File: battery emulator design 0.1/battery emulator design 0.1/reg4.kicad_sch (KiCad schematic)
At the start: 12 parts, among them U7 LM741, U8 LM317_TO-220

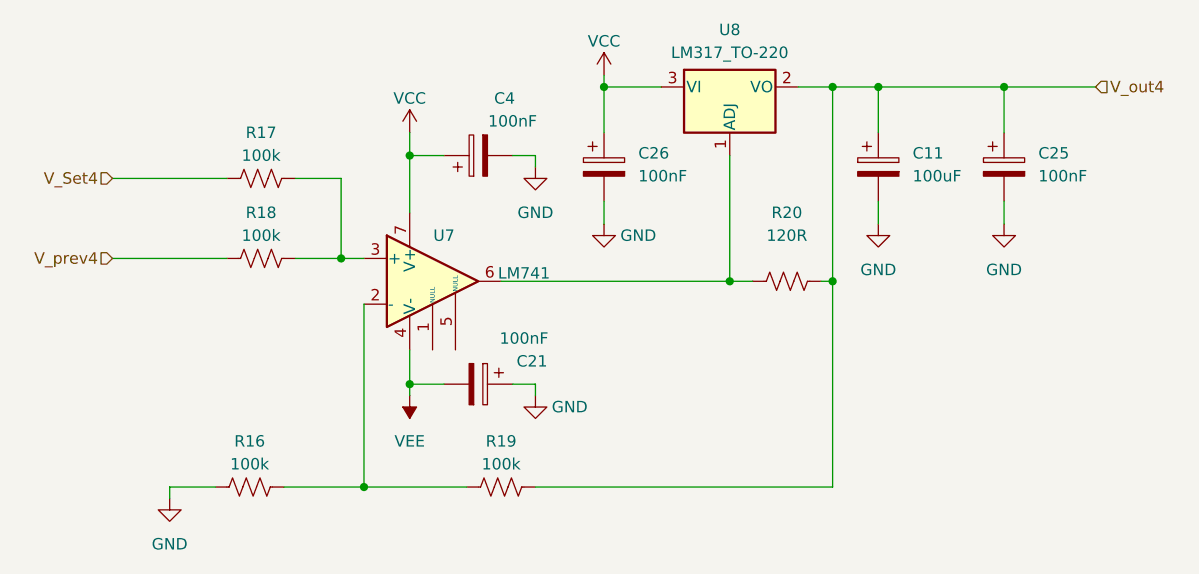
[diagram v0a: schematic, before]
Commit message: added pots to voltage buffers, other minor changes
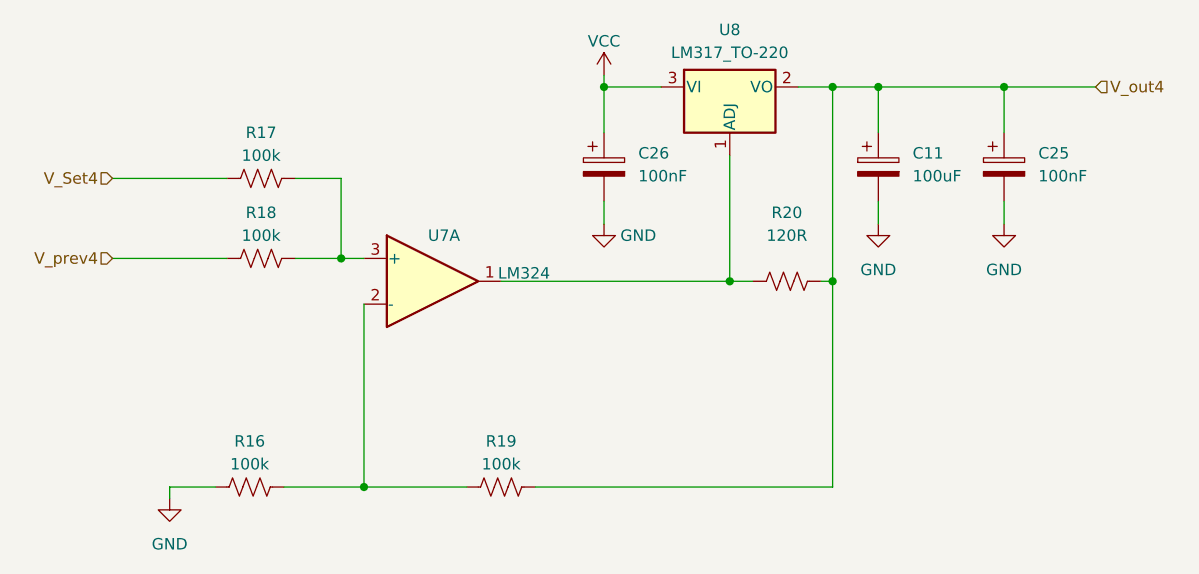
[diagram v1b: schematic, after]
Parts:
- removed C21, C4: 100nF, Capacitor_THT:C_Disc_D3.4mm_W2.1mm_P2.50mm, symbol Device:C_Polarized
- U7: value LM741 -> LM324; symbol Amplifier_Operational:LM741 -> Amplifier_Operational:LM324
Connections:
- net VCC: no longer U7.7 (V+)
- net at R20.2, U8.1 (ADJ): now also U7.1; no longer U7.6
- removed net VEE: U7.4 (V-)
